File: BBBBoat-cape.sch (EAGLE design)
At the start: 34 parts

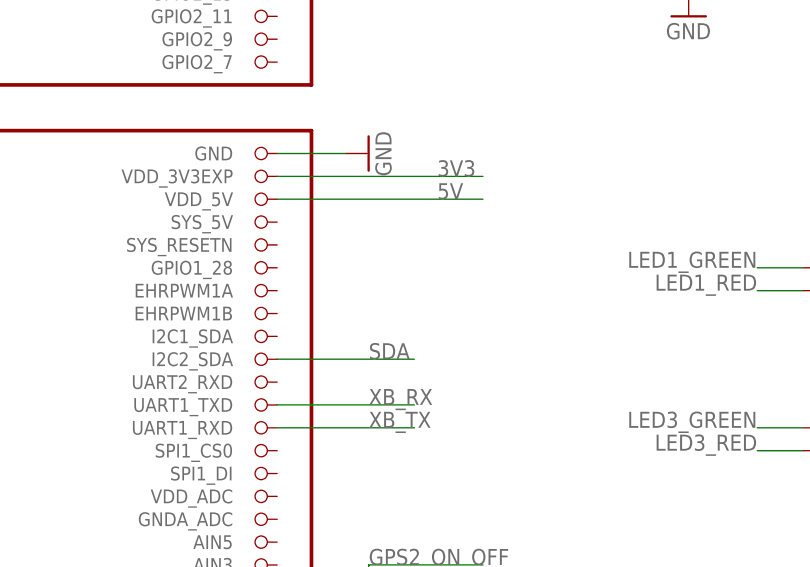
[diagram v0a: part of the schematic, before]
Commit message: change PWM pin
the pwm B pins currently don't work in the PyBBIO library
so PWM2B was switched to PWM1A
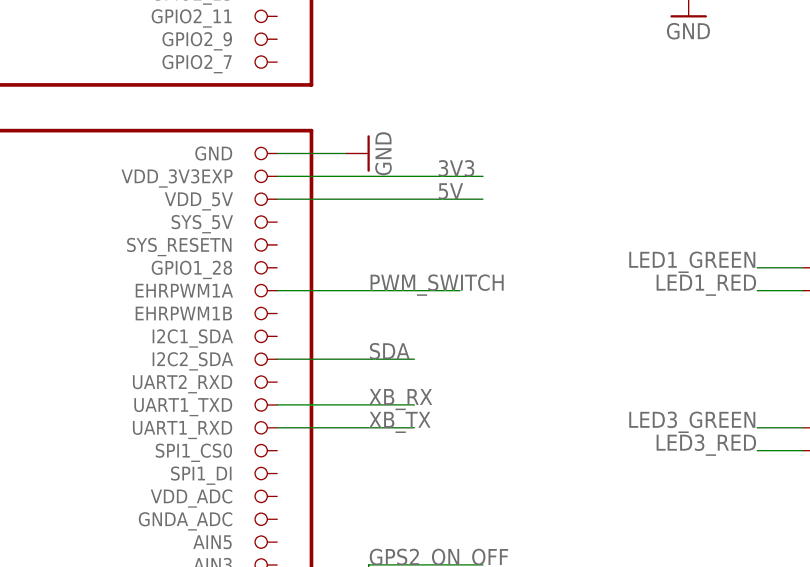
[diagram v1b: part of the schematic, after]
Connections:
- new net PWM_SWITCH: U$1.EHRPWM1A
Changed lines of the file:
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@@
+</segment>
+</net>
+<net name="PWM_SWITCH" class="0">
+<segment>
+<pinref part="U$1" gate="G$1" pin="EHRPWM1A"/>
+<wire x1="88.9" y1="71.12" x2="109.22" y2="71.12" width="0.1524" layer="91"/>
+<label x="99.06" y="71.12" size="1.778" layer="95"/>
 </segment>
 </net>
